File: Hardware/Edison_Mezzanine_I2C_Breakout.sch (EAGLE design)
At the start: 21 parts, among them U2 PCA9306

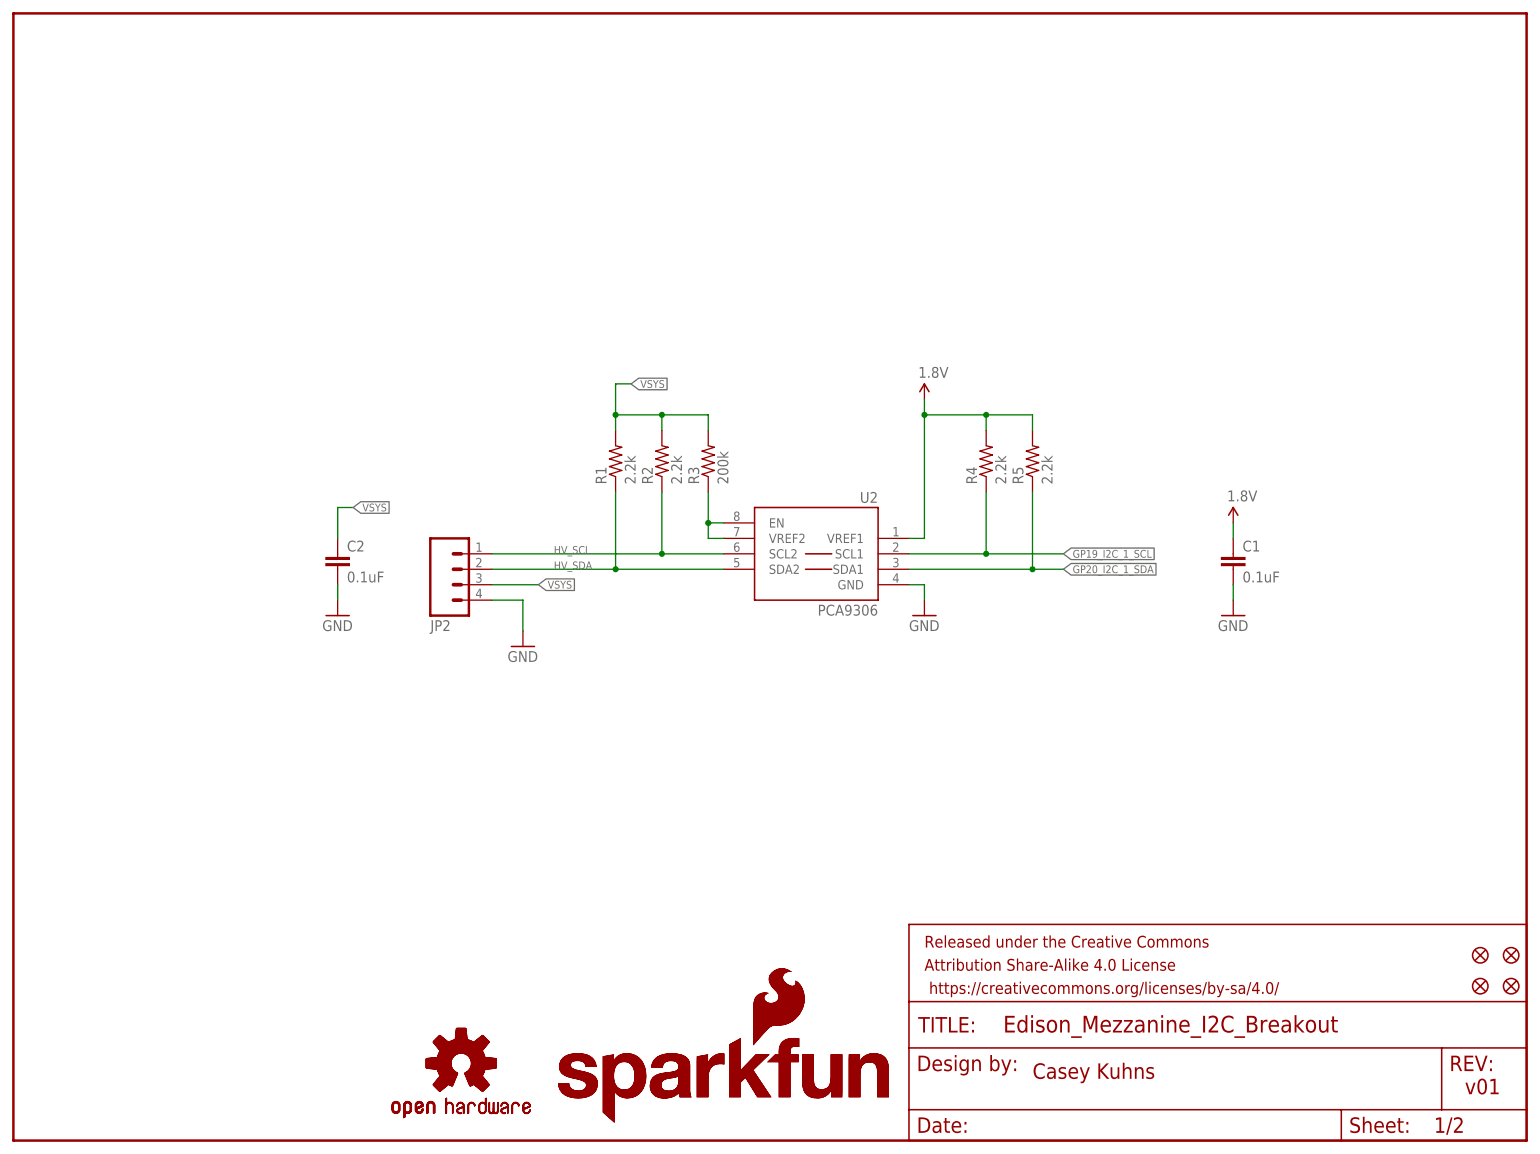
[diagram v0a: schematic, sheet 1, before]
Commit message: corrected labels, added 3.3v regulator and corrected DCIN pin
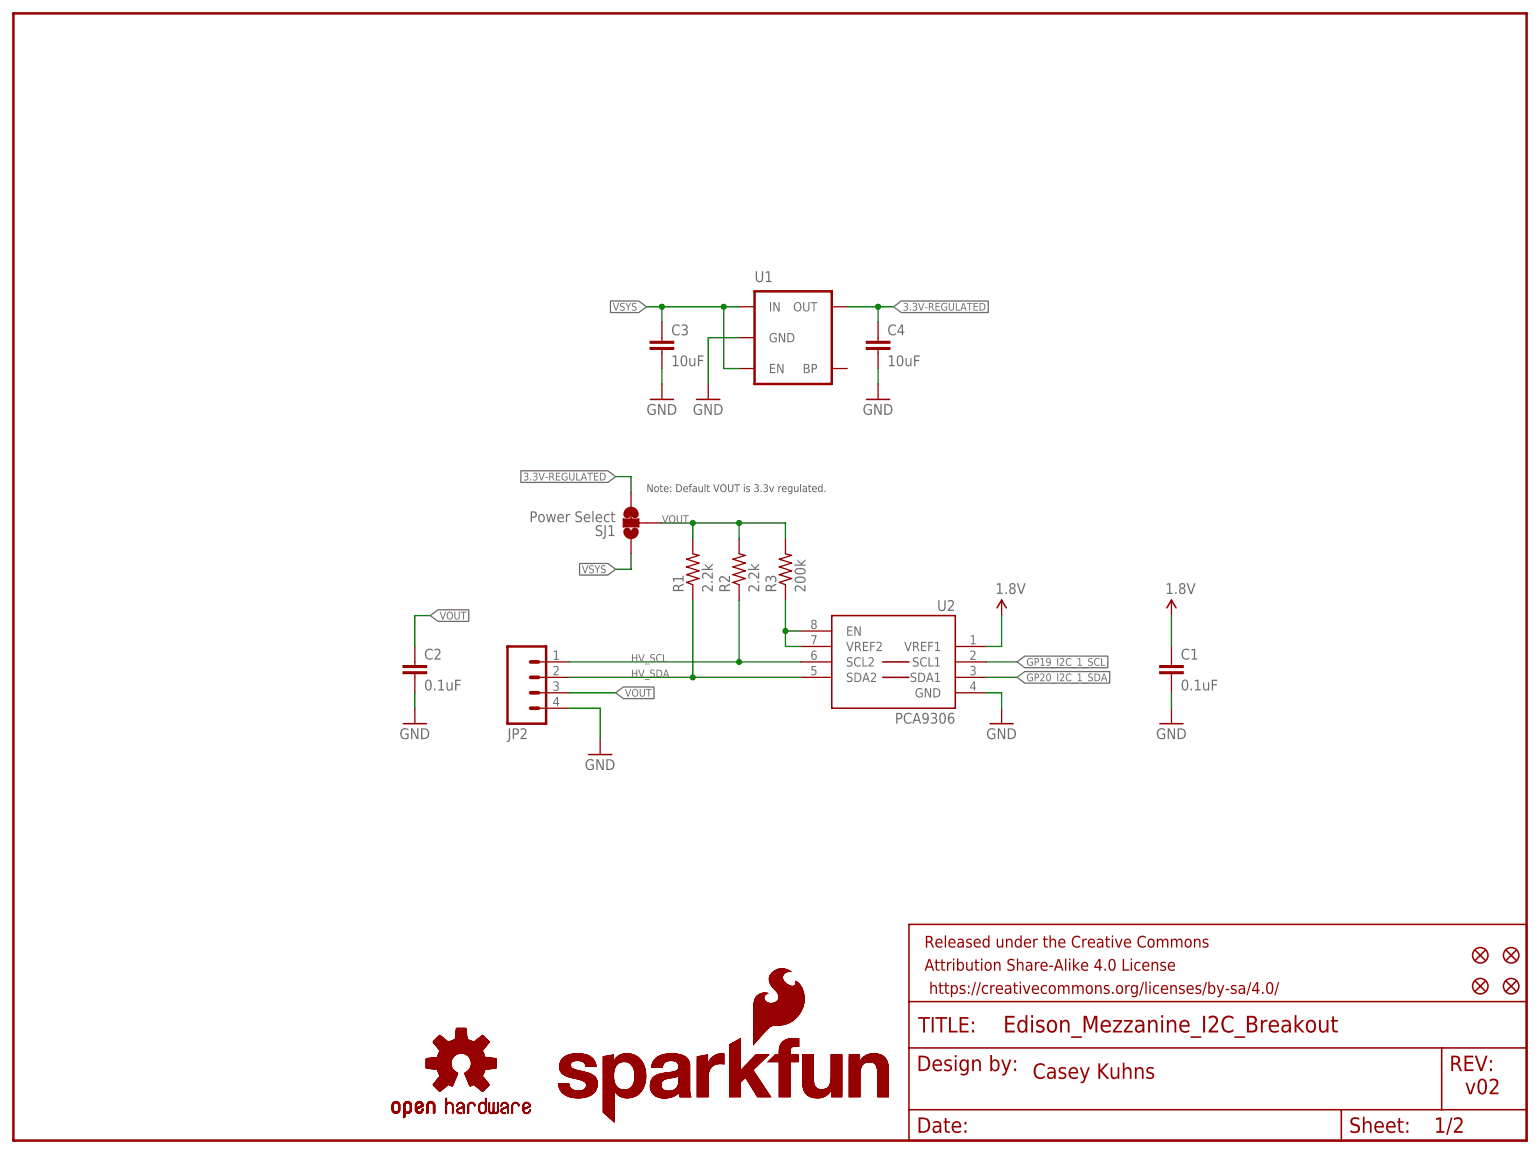
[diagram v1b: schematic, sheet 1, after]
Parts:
- removed R4, R5: 2.2k, SparkFun-Resistors:2.2KOHM1/10W1%(0603)
- added C3, C4: 10uF, SparkFun-Capacitors:10UF-6.3V-20%(1206)
- added SJ1: Power Select, SparkFun-Passives:JUMPER-PAD-3-2OF3_NC_BY_TRACE
- added U1: (no value), SparkFun-PowerIC:MIC52053.3V
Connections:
- new net 3.3V-REGULATED: C4.1, SJ1.3, U1.OUT
- new net DCIN: U$2.DCIN, U$3.DCIN
- new net VOUT: C2.1, JP2.3, R1.2, R2.2, R3.2, SJ1.2
- net 1.8V: no longer R4.2, R5.2
- net GND: now also C3.2, C4.2, U1.GND
- net GP19_I2C_1_SCL: no longer R4.1
- net GP20_I2C_1_SDA: no longer R5.1
- net VSYS: now also C3.1, SJ1.1, U1.EN, U1.IN; no longer C2.1, JP2.3, R1.2, R2.2, R3.2
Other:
- note added: "Note: Default VOUT is 3.3v regulated."
- note added: "v02"
- note removed: "v01"
- moved on the sheet: C1, C2, JP2, R1, R2, R3, U2
